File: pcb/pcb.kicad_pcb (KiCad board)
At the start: 2 copper layers, 115.2 x 76.8 mm, 27 parts, among them J1 TYPE-C-31-M-12, SW1 SW_Push, SW10 SW_Push, SW11 SW_Push, SW12 SW_Push, SW13 SW_Push, SW14 SW_Push, SW15 SW_Push, SW16 SW_Push, SW17 SW_Push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

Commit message: parts align (without trrs jack)
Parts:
- added C1: 22p, SMD:2012M, B.Cu at (72.3, 31.2)
- added C2: 22p, SMD:2012M, B.Cu at (80.1, 31.2)
- added C3: 1u, SMD:2012M, B.Cu at (88.9, 17.7)
- added C4: 1u, SMD:2012M, B.Cu at (101.8, 21.4)
- added D1: D, SMD:SOD123, B.Cu at (17.3, 11.3)
- added D10: D, SMD:SOD123, B.Cu at (59.5, 30.5)
- added D11: D, SMD:SOD123, B.Cu at (94.1, 30.5)
- added D12: D, SMD:SOD123, B.Cu at (97.9, 30.5)
- added D13: D, SMD:SOD123, B.Cu at (17.3, 49.7)
- added D14: D, SMD:SOD123, B.Cu at (21.1, 49.7)
- added D15: D, SMD:SOD123, B.Cu at (55.7, 49.7)
- added D16: D, SMD:SOD123, B.Cu at (59.5, 49.7)
- added D17: D, SMD:SOD123, B.Cu at (94.1, 49.7)
- added D18: D, SMD:SOD123, B.Cu at (97.9, 49.7)
- added D19: D, SMD:SOD123, B.Cu at (17.3, 68.9)
- added D2: D, SMD:SOD123, B.Cu at (21.1, 11.3)
- added D20: D, SMD:SOD123, B.Cu at (21.1, 68.9)
- added D21: D, SMD:SOD123, B.Cu at (55.7, 68.9)
- added D22: D, SMD:SOD123, B.Cu at (59.5, 68.9)
- added D23: D, SMD:SOD123, B.Cu at (94.1, 68.9)
- added D24: D, SMD:SOD123, B.Cu at (97.9, 68.9)
- added D3: D, SMD:SOD123, B.Cu at (55.7, 11.3)
- added D4: D, SMD:SOD123, B.Cu at (59.5, 11.3)
- added D5: D, SMD:SOD123, B.Cu at (94.1, 11.3)
- added D6: D, SMD:SOD123, B.Cu at (97.9, 11.3)
- added D7: D, SMD:SOD123, B.Cu at (17.3, 30.5)
- added D8: D, SMD:SOD123, B.Cu at (21.1, 30.5)
- added D9: D, SMD:SOD123, B.Cu at (55.7, 30.5)
- added R1: 10k, SMD:2012M, B.Cu at (68.5, 13.7)
- added R2: 22, SMD:2012M, B.Cu at (96.0, 18.6)
- added R3: 22, SMD:2012M, B.Cu at (96.0, 15.5)
- added R4: 5.1k, SMD:2012M, B.Cu at (101.8, 14.8)
- added R5: 5.1k, SMD:2012M, B.Cu at (101.8, 19.3)
- J1: footprint USB_Type-C:HRO_TYPE-C-31-M-12 -> USB_Type-C:TYPE-C-31-M-12; moved to B.Cu
- SW1, SW10, SW11, SW12, SW13, SW14, SW15, SW16, SW17, SW18, SW19, SW2, SW20, SW21, SW22, SW23, SW24, SW3, SW4, SW5, SW6, SW7, SW8, SW9: footprint Cherry_MX:1u_socket -> Cherry_MX:1u
- moved J1 63.3 mm to (115.2, 17.0), turned to 90 degrees
- moved U1 17.8 mm to (78.3, 17.7), turned to 180 degrees
- moved Y1 12.0 mm to (76.8, 31.2)
- turned SW10 to 0 degrees
- turned SW11 to 0 degrees
- turned SW12 to 0 degrees
- turned SW19 to 0 degrees
- turned SW20 to 0 degrees
- turned SW21 to 0 degrees
- turned SW22 to 0 degrees
- turned SW23 to 0 degrees
- turned SW24 to 0 degrees
- turned SW7 to 0 degrees
- turned SW8 to 0 degrees
- turned SW9 to 0 degrees
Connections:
- SW1 pad 2: (no net) -> Net-(D1-Pad2)
- SW10 pad 2: (no net) -> Net-(D10-Pad2)
- SW11 pad 2: (no net) -> Net-(D11-Pad2)
- SW12 pad 2: (no net) -> Net-(D12-Pad2)
- SW13 pad 2: (no net) -> Net-(D13-Pad2)
- SW14 pad 2: (no net) -> Net-(D14-Pad2)
- SW15 pad 2: (no net) -> Net-(D15-Pad2)
- SW16 pad 2: (no net) -> Net-(D16-Pad2)
- SW17 pad 2: (no net) -> Net-(D17-Pad2)
- SW18 pad 2: (no net) -> Net-(D18-Pad2)
- SW19 pad 2: (no net) -> Net-(D19-Pad2)
- SW2 pad 2: (no net) -> Net-(D2-Pad2)
- SW20 pad 2: (no net) -> Net-(D20-Pad2)
- SW21 pad 2: (no net) -> Net-(D21-Pad2)
- SW22 pad 2: (no net) -> Net-(D22-Pad2)
- SW23 pad 2: (no net) -> Net-(D23-Pad2)
- SW24 pad 2: (no net) -> Net-(D24-Pad2)
- SW3 pad 2: (no net) -> Net-(D3-Pad2)
- SW4 pad 2: (no net) -> Net-(D4-Pad2)
- SW5 pad 2: (no net) -> Net-(D5-Pad2)
- SW6 pad 2: (no net) -> Net-(D6-Pad2)
- SW7 pad 2: (no net) -> Net-(D7-Pad2)
- SW8 pad 2: (no net) -> Net-(D8-Pad2)
- SW9 pad 2: (no net) -> Net-(D9-Pad2)
- U1 pad 3: (no net) -> D-
- U1 pad 33: (no net) -> Net-(R1-Pad2)
- U1 pad 38: (no net) -> R3
- U1 pad 39: (no net) -> R2
- U1 pad 4: (no net) -> D+
- U1 pad 40: (no net) -> R1
- U1 pad 41: (no net) -> R0
- U1 pad 6: (no net) -> Net-(C3-Pad1)
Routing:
- net R1: track 0.00 -> 81.9 mm
- net R3: track 0.00 -> 80.6 mm
- net R2: track 0.00 -> 80.6 mm
- net C5: track 0.00 -> 57.6 mm
- net C4: track 0.00 -> 57.6 mm
- net C3: track 0.00 -> 57.6 mm
- net C2: track 0.00 -> 57.6 mm
- net C1: track 0.00 -> 57.6 mm
- net C0: track 0.00 -> 57.6 mm
- net R0: track 0.00 -> 46.0 mm
- net GND: track 0.00 -> 29.7 mm
- net Net-(D24-Pad2): track 0.00 -> 14.9 mm
- net Net-(D20-Pad2): track 0.00 -> 14.9 mm
- net Net-(D8-Pad2): track 0.00 -> 14.9 mm
- net Net-(D12-Pad2): track 0.00 -> 14.9 mm
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- added copper zone on B.Cu, net Net-(J1-PadA6)
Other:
- net class Default: trace_width 0.25 -> 0.3

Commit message: routing done
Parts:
- added J2: AudioJack4, Phone_Connector:MJ-4PP-9, B.Cu at (115.2, 38.4)
- added J3: AudioJack4, Phone_Connector:MJ-4PP-9, B.Cu at (0.00, 38.4)
- moved R1 2.17 mm to (70.4, 12.7), turned to 270 degrees
- moved C3 0.80 mm to (88.9, 18.5)
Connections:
- U1 pad 10: C2 -> (no net)
- U1 pad 11: C3 -> (no net)
- U1 pad 18: (no net) -> SCL
- U1 pad 19: (no net) -> SDA
- U1 pad 26: (no net) -> R3
- U1 pad 27: (no net) -> R2
- U1 pad 28: C4 -> R1
- U1 pad 29: C5 -> C2
- U1 pad 30: (no net) -> C1
- U1 pad 31: (no net) -> C0
- U1 pad 36: (no net) -> C3
- U1 pad 38: R3 -> C5
- U1 pad 39: R2 -> C4
- U1 pad 40: R1 -> (no net)
- U1 pad 8: C0 -> (no net)
- U1 pad 9: C1 -> (no net)
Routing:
- net VCC: track 5.50 -> 211.3 mm, vias 0 -> 4
- net GND: track 29.7 -> 216.8 mm, vias 0 -> 7
- net SCL: track 0.00 -> 142.9 mm, vias 0 -> 3
- net SDA: track 0.00 -> 137.8 mm, vias 0 -> 3
- net C0: track 57.6 -> 136.1 mm
- net R3: track 80.6 -> 146.2 mm, vias 0 -> 2
- net C5: track 57.6 -> 115.9 mm, vias 0 -> 1
- net R0: track 46.0 -> 97.6 mm
- net C1: track 57.6 -> 109.1 mm
- net R2: track 80.6 -> 126.7 mm, vias 0 -> 2
- net C4: track 57.6 -> 103.3 mm, vias 0 -> 1
- net R1: track 81.9 -> 119.5 mm, vias 0 -> 2
- net C2: track 57.6 -> 89.5 mm
- net C3: track 57.6 -> 73.8 mm, vias 0 -> 1
- net Net-(R1-Pad2): track 0.00 -> 1.87 mm

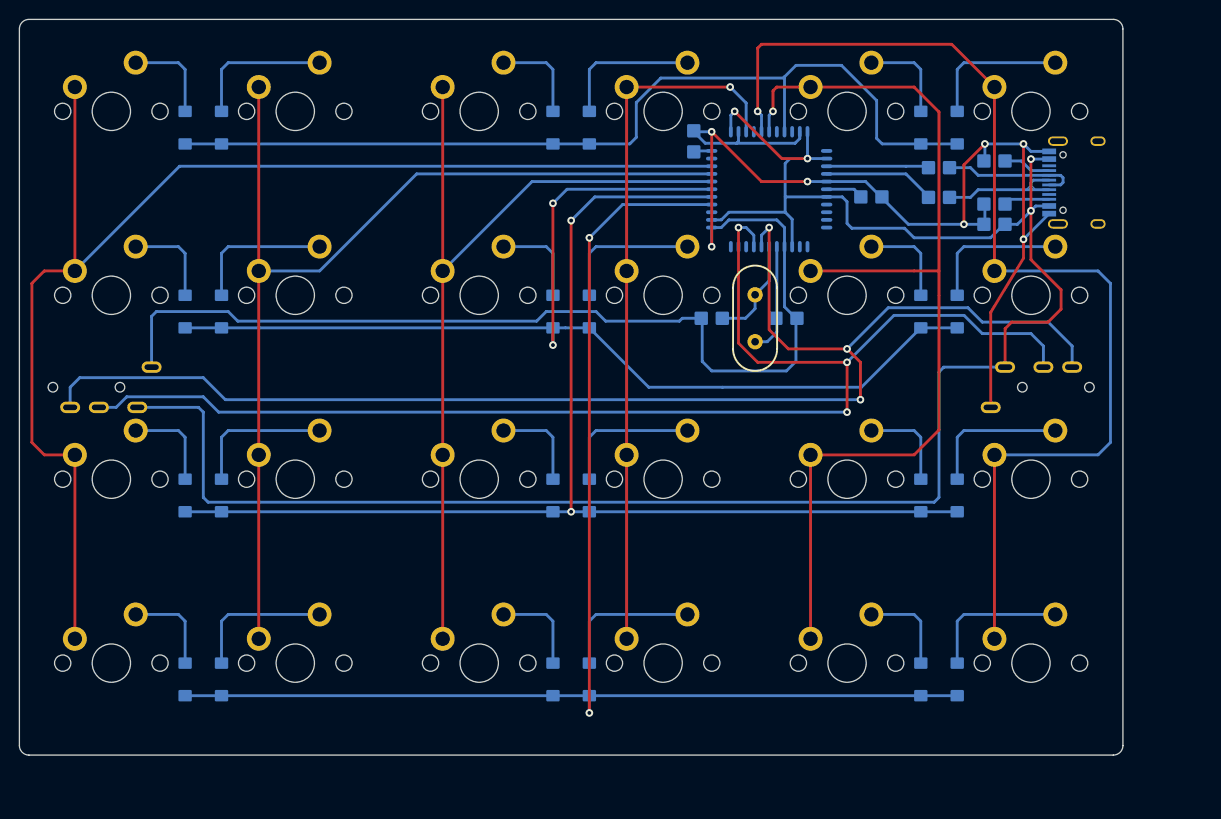
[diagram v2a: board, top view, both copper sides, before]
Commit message: routing with curve
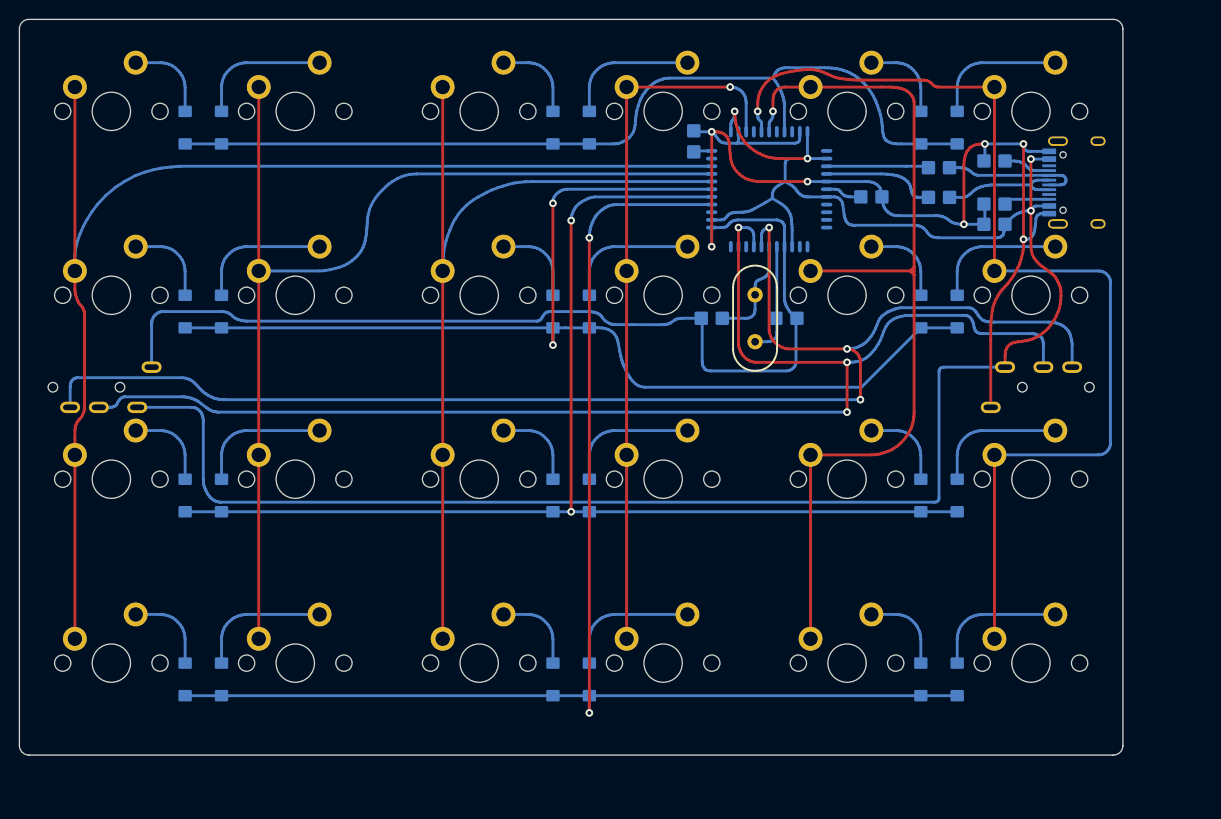
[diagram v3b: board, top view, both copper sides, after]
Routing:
- net C4: track 103.3 -> 96.6 mm
- net C5: track 115.9 -> 110.8 mm
- net C0: track 136.1 -> 130.9 mm
- net C2: track 89.5 -> 91.3 mm
- net C1: track 109.1 -> 110.7 mm
- net R0: track 97.6 -> 95.9 mm
- net R1: track 119.5 -> 121.0 mm
- net GND: track 216.8 -> 218.2 mm
- net SCL: track 142.9 -> 144.2 mm
- net SDA: track 137.8 -> 139.0 mm
- net VCC: track 211.3 -> 210.6 mm
- net Net-(D19-Pad2): track 9.83 -> 9.11 mm
- net Net-(D8-Pad2): track 14.9 -> 14.2 mm
- net Net-(D22-Pad2): track 14.9 -> 14.2 mm
- net Net-(D21-Pad2): track 9.83 -> 9.11 mm
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- removed copper zone on B.Cu, net Net-(J1-PadA6)

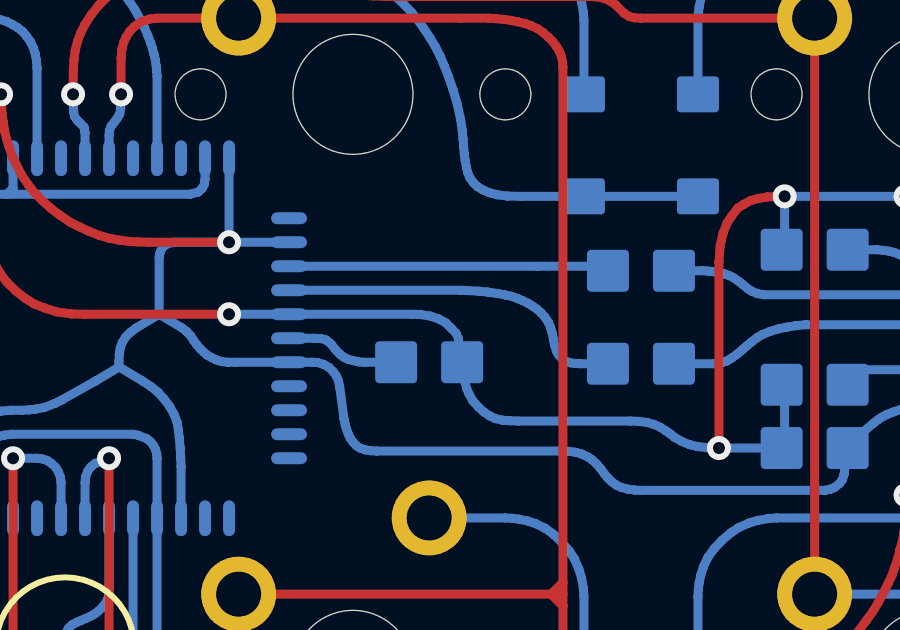
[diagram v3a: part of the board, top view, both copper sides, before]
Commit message: same length usb routing
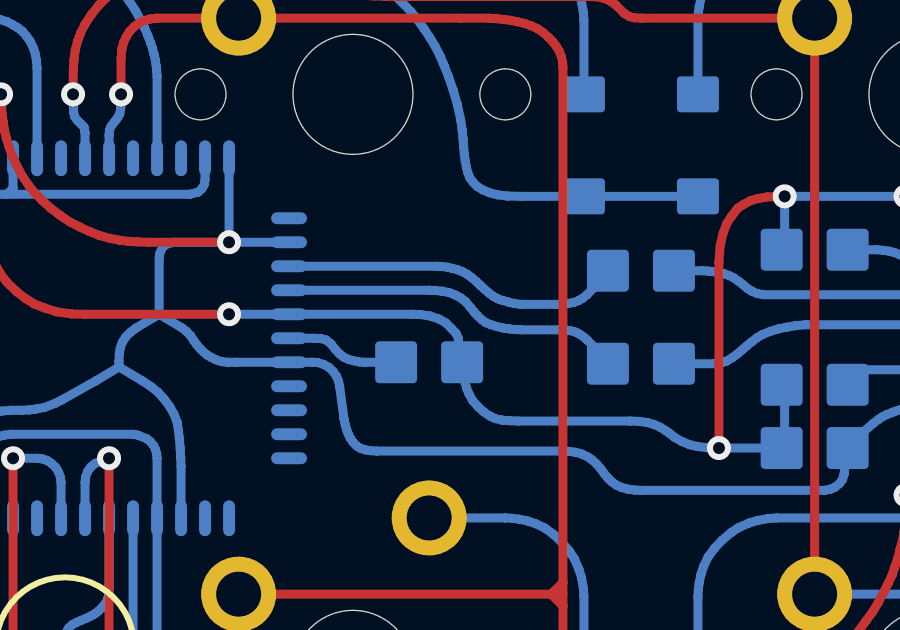
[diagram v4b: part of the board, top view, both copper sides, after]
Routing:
- net D-: track 10.7 -> 11.5 mm
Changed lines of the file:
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@@
   (general
     (thickness 1.6)
-    (drawings 8)
-    (tracks 1726)
+    (drawings 9)
+    (tracks 1750)
     (zones 0)
     (modules 62)
@@
       (net 9 "Net-(C1-Pad1)"))
   )
+  (gr_line (start 94.9 17.03) (end 90 17.03) (layer F.Fab) (width 0.15))
   (gr_line (start 1 0) (end 114.2 0) (layer Edge.Cuts) (width 0.05))
   (gr_arc (start 114.2 1) (end 115.2 1) (angle -90) (layer Edge.Cuts) (width 0.05))
@@
   (segment (start 107.5 18.78) (end 103.29 18.78) (width 0.3) (layer B.Cu) (net 15))
   (segment (start 72.27 13.73) (end 70.4 13.73) (width 0.3) (layer B.Cu) (net 16))
-  (segment (start 90 16.13) (end 84.27 16.13) (width 0.3) (layer B.Cu) (net 17))
-  (segment (start 95 18.58) (end 93.97 18.58) (width 0.3) (layer B.Cu) (net 17))
-  (segment (start 93.97 18.58) (end 93.81 18.57) (width 0.3) (layer B.Cu) (net 17))
-  (segment (start 93.81 18.57) (end 93.65 18.55) (width 0.3) (layer B.Cu) (net 17))
-  (segment (start 93.65 18.55) (end 93.5 18.5) (width 0.3) (layer B.Cu) (net 17))
-  (segment (start 93.5 18.5) (end 93.37 18.41) (width 0.3) (layer B.Cu) (net 17))
-  (segment (start 93.37 18.41) (end 93.26 18.29) (width 0.3) (layer B.Cu) (net 17))
-  (segment (start 93.26 18.29) (end 93.18 18.15) (width 0.3) (layer B.Cu) (net 17))
-  (segment (start 93.18 18.15) (end 93.12 17.96) (width 0.3) (layer B.Cu) (net 17))
-  (segment (start 93.12 17.96) (end 93.08 17.75) (width 0.3) (layer B.Cu) (net 17))
-  (segment (start 93.08 17.75) (end 93.04 17.55) (width 0.3) (layer B.Cu) (net 17))
-  (segment (start 93.04 17.55) (end 92.99 17.38) (width 0.3) (layer B.Cu) (net 17))
-  (segment (start 92.99 17.38) (end 92.91 17.19) (width 0.3) (layer B.Cu) (net 17))
-  (segment (start 92.91 17.19) (end 92.81 17.04) (width 0.3) (layer B.Cu) (net 17))
-  (segment (start 92.81 17.04) (end 92.68 16.89) (width 0.3) (layer B.Cu) (net 17))
-  (segment (start 92.68 16.89) (end 92.53 16.76) (width 0.3) (layer B.Cu) (net 17))
-  (segment (start 92.53 16.76) (end 92.39 16.66) (width 0.3) (layer B.Cu) (net 17))
-  (segment (start 92.39 16.66) (end 92.23 16.56) (width 0.3) (layer B.Cu) (net 17))
-  (segment (start 92.23 16.56) (end 92.04 16.47) (width 0.3) (layer B.Cu) (net 17))
-  (segment (start 92.04 16.47) (end 91.88 16.4) (width 0.3) (layer B.Cu) (net 17))
-  (segment (start 91.88 16.4) (end 91.68 16.33) (width 0.3) (layer B.Cu) (net 17))
-  (segment (start 91.68 16.33) (end 91.49 16.29) (width 0.3) (layer B.Cu) (net 17))
-  (segment (start 91.49 16.29) (end 91.23 16.24) (width 0.3) (layer B.Cu) (net 17))
-  (segment (start 91.23 16.24) (end 90.89 16.19) (width 0.3) (layer B.Cu) (net 17))
-  (segment (start 90.89 16.19) (end 90.58 16.16) (width 0.3) (layer B.Cu) (net 17))
-  (segment (start 90.58 16.16) (end 90 16.13) (width 0.3) (layer B.Cu) (net 17))
-  (segment (start 84.27 15.33) (end 92.55 15.33) (width 0.3) (layer B.Cu) (net 18))
-  (segment (start 92.55 15.33) (end 95 15.33) (width 0.3) (layer B.Cu) (net 18))
+  (segment (start 94.2 17.78) (end 95 18.58) (width 0.3) (layer B.Cu) (net 17))
+  (segment (start 94.08 17.68) (end 94.2 17.78) (width 0.3) (layer B.Cu) (net 17))
+  (segment (start 93.95 17.59) (end 94.08 17.68) (width 0.3) (layer B.Cu) (net 17))
+  (segment (start 90.54 16.97) (end 90.69 17.11) (width 0.3) (layer B.Cu) (net 17))
+  (segment (start 91.62 17.42) (end 91.81 17.44) (width 0.3) (layer B.Cu) (net 17))
+  (segment (start 90.42 16.83) (end 90.54 16.97) (width 0.3) (layer B.Cu) (net 17))
+  (segment (start 90.69 17.11) (end 90.83 17.21) (width 0.3) (layer B.Cu) (net 17))
+  (segment (start 90.14 16.5) (end 90.31 16.69) (width 0.3) (layer B.Cu) (net 17))
+  (segment (start 90.31 16.69) (end 90.42 16.83) (width 0.3) (layer B.Cu) (net 17))
+  (segment (start 89.61 16.21) (end 89.82 16.29) (width 0.3) (layer B.Cu) (net 17))
+  (segment (start 89.82 16.29) (end 90 16.39) (width 0.3) (layer B.Cu) (net 17))
+  (segment (start 89.15 16.14) (end 89.37 16.16) (width 0.3) (layer B.Cu) (net 17))
+  (segment (start 93.26 17.45) (end 93.5 17.46) (width 0.3) (layer B.Cu) (net 17))
+  (segment (start 88.95 16.13) (end 89.15 16.14) (width 0.3) (layer B.Cu) (net 17))
+  (segment (start 90 16.39) (end 90.14 16.5) (width 0.3) (layer B.Cu) (net 17))
+  (segment (start 84.27 16.13) (end 88.95 16.13) (width 0.3) (layer B.Cu) (net 17))
+  (segment (start 90.83 17.21) (end 91 17.28) (width 0.3) (layer B.Cu) (net 17))
+  (segment (start 91 17.28) (end 91.2 17.34) (width 0.3) (layer B.Cu) (net 17))
+  (segment (start 91.2 17.34) (end 91.41 17.39) (width 0.3) (layer B.Cu) (net 17))
+  (segment (start 91.41 17.39) (end 91.62 17.42) (width 0.3) (layer B.Cu) (net 17))
+  (segment (start 91.81 17.44) (end 92 17.45) (width 0.3) (layer B.Cu) (net 17))
+  (segment (start 93.66 17.48) (end 93.81 17.52) (width 0.3) (layer B.Cu) (net 17))
+  (segment (start 92 17.45) (end 93.26 17.45) (width 0.3) (layer B.Cu) (net 17))
+  (segment (start 93.5 17.46) (end 93.66 17.48) (width 0.3) (layer B.Cu) (net 17))
+  (segment (start 89.37 16.16) (end 89.61 16.21) (width 0.3) (layer B.Cu) (net 17))
+  (segment (start 93.81 17.52) (end 93.95 17.59) (width 0.3) (layer B.Cu) (net 17))
+  (segment (start 94.05 16.4) (end 94.2 16.28) (width 0.3) (layer B.Cu) (net 18))
+  (segment (start 93.91 16.48) (end 94.05 16.4) (width 0.3) (layer B.Cu) (net 18))
+  (segment (start 90.36 15.71) (end 90.51 15.84) (width 0.3) (layer B.Cu) (net 18))
+  (segment (start 90.07 15.52) (end 90.21 15.6) (width 0.3) (layer B.Cu) (net 18))
+  (segment (start 89.9 15.45) (end 90.07 15.52) (width 0.3) (layer B.Cu) (net 18))
+  (segment (start 90.51 15.84) (end 90.64 15.96) (width 0.3) (layer B.Cu) (net 18))
+  (segment (start 93.4 16.59) (end 93.58 16.57) (width 0.3) (layer B.Cu) (net 18))
+  (segment (start 84.27 15.33) (end 89.16 15.33) (width 0.3) (layer B.Cu) (net 18))
+  (segment (start 90.64 15.96) (end 90.79 16.1) (width 0.3) (layer B.Cu) (net 18))
+  (segment (start 89.16 15.33) (end 89.35 15.34) (width 0.3) (layer B.Cu) (net 18))
+  (segment (start 90.79 16.1) (end 90.93 16.22) (width 0.3) (layer B.Cu) (net 18))
+  (segment (start 89.35 15.34) (end 89.54 15.36) (width 0.3) (layer B.Cu) (net 18))
+  (segment (start 89.71 15.4) (end 89.9 15.45) (width 0.3) (layer B.Cu) (net 18))
+  (segment (start 90.93 16.22) (end 91.09 16.34) (width 0.3) (layer B.Cu) (net 18))
+  (segment (start 89.54 15.36) (end 89.71 15.4) (width 0.3) (layer B.Cu) (net 18))
+  (segment (start 94.2 16.28) (end 95 15.48) (width 0.3) (layer B.Cu) (net 18))
+  (segment (start 91.39 16.47) (end 91.57 16.52) (width 0.3) (layer B.Cu) (net 18))
+  (segment (start 91.57 16.52) (end 91.77 16.57) (width 0.3) (layer B.Cu) (net 18))
+  (segment (start 91.24 16.42) (end 91.39 16.47) (width 0.3) (layer B.Cu) (net 18))
+  (segment (start 91.77 16.57) (end 92 16.6) (width 0.3) (layer B.Cu) (net 18))
+  (segment (start 92 16.6) (end 93.22 16.6) (width 0.3) (layer B.Cu) (net 18))
+  (segment (start 91.09 16.34) (end 91.24 16.42) (width 0.3) (layer B.Cu) (net 18))
+  (segment (start 93.75 16.54) (end 93.91 16.48) (width 0.3) (layer B.Cu) (net 18))
+  (segment (start 93.22 16.6) (end 93.4 16.59) (width 0.3) (layer B.Cu) (net 18))
+  (segment (start 90.21 15.6) (end 90.36 15.71) (width 0.3) (layer B.Cu) (net 18))
+  (segment (start 93.58 16.57) (end 93.75 16.54) (width 0.3) (layer B.Cu) (net 18))
   (segment (start 12.14 4.52) (end 14.68 4.52) (width 0.3) (layer B.Cu) (net 19))
   (segment (start 17.3 9.6) (end 17.3 7.14) (width 0.3) (layer B.Cu) (net 19))
